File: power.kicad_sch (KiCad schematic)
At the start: 33 parts, among them J12 Conn_02x02_Odd_Even, J13 Barrel_Jack_MountingPin, Q5 DMP3056L-13, SW1 Power, U10 TPS54302

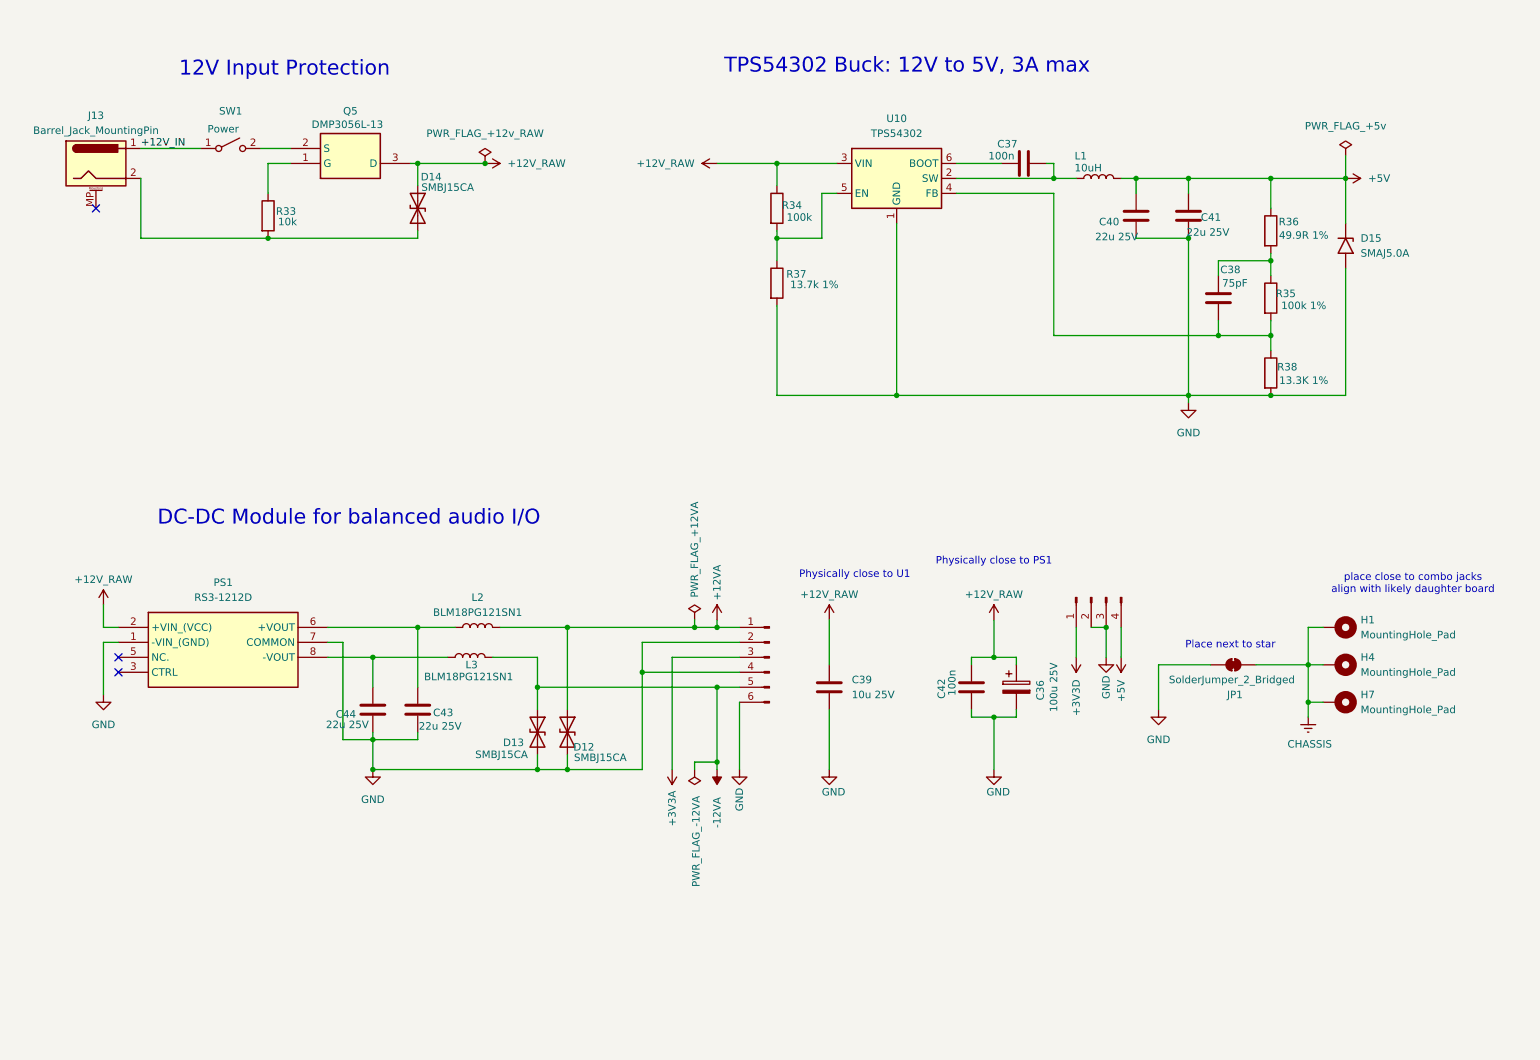
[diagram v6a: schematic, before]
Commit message: added 3d models
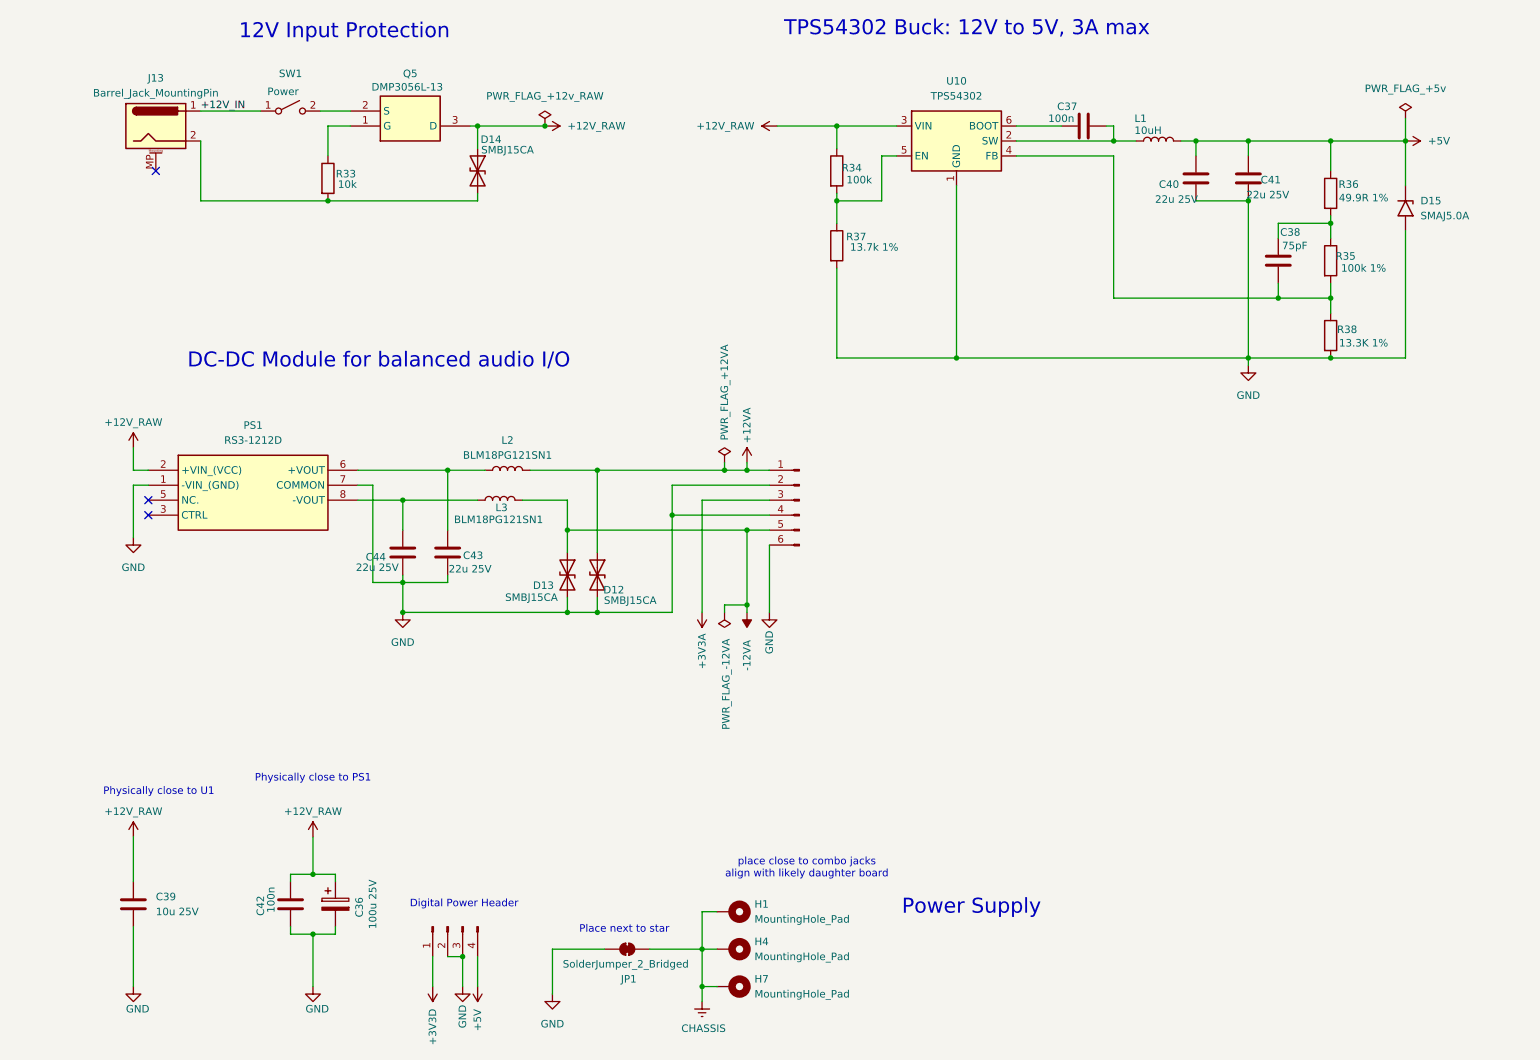
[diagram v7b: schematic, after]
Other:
- note added: "Digital Power Header"
- note added: "Power Supply"
- moved on the sheet: C36, C37, C38, C39, C40, C41, C42, C43, C44, D12, D13, D14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

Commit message: fix j8 value
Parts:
- J8: value ~ -> Conn_02x03
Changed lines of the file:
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@@
 			)
 		)
-		(property "Value" "~"
+		(property "Value" "Conn_02x03"
 			(at 142.494 116.332 90)
 			(effects
